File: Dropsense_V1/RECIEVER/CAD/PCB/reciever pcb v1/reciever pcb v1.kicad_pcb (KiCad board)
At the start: 2 copper layers, 50 x 60 mm, 27 parts, among them J1 1.8inch TFT connector, J2 USB_B_Micro, J3 Battery connector, SW1 EN SW, SW2 IO0 SW, U1 ESP32-S3-WROOM-1, U2 TP4056, U3 ME6211

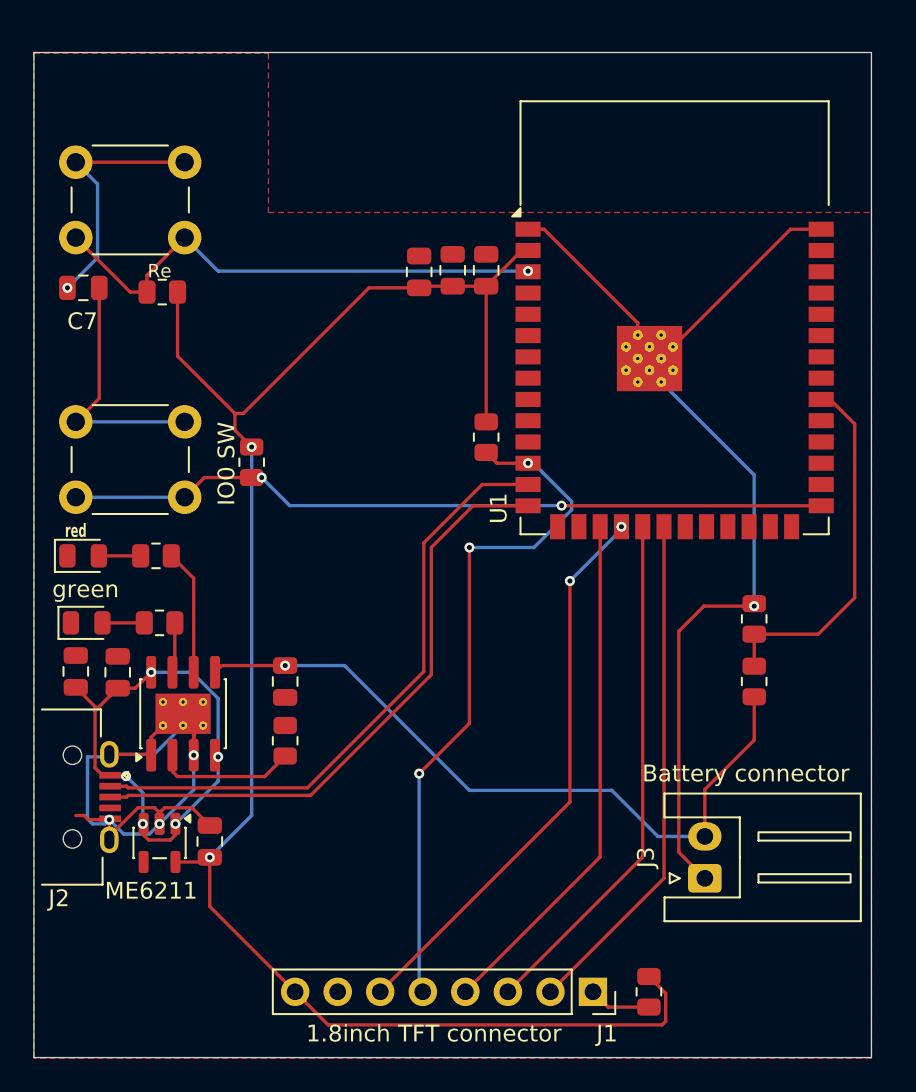
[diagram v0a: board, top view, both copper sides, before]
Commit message: PCB improvement
updated and polished both the pcbs of the sender and reciever mainly woked on moving viases away from smd components
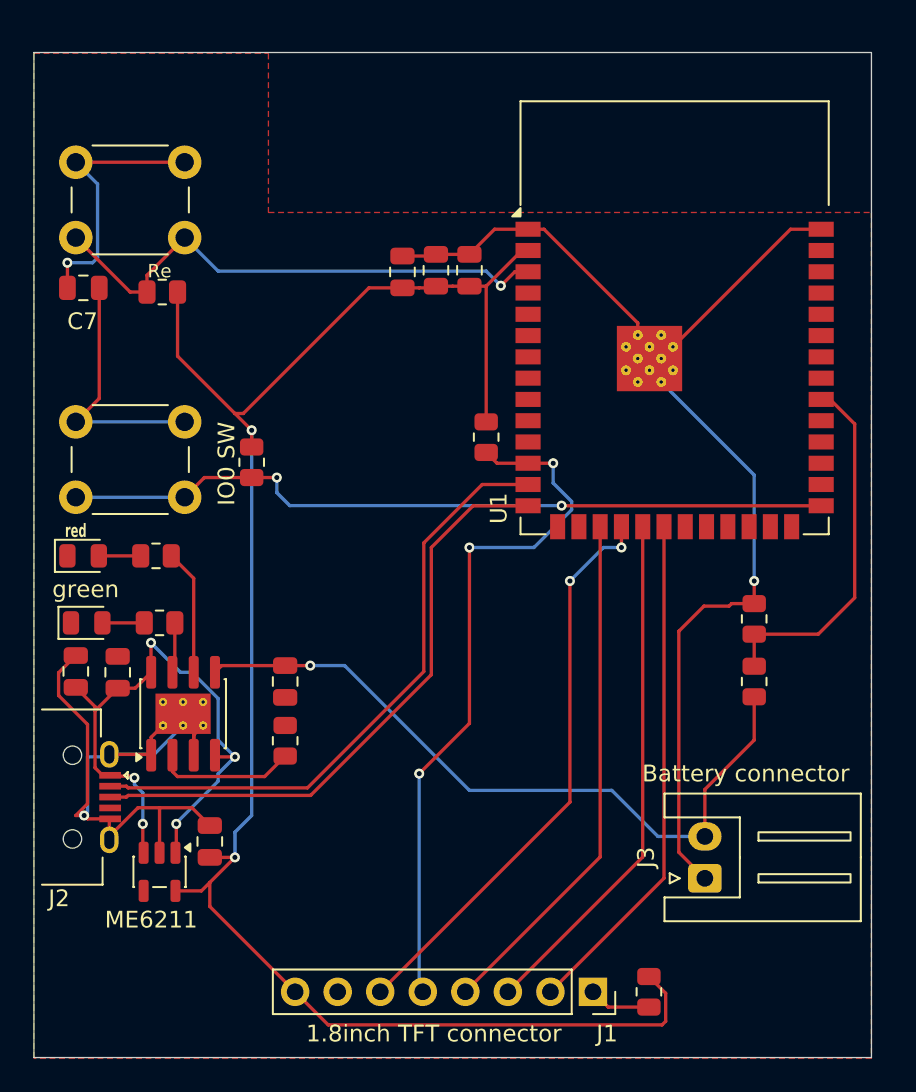
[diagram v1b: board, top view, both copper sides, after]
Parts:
- moved U3 1.72 mm to (109.5, 97.9)
- moved C4 1.00 mm to (124.0, 62.0)
- moved C5 1.00 mm to (126.0, 62.0)
- moved C6 1.00 mm to (128.0, 62.0)
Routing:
- net GND: track 114.7 -> 126.6 mm, vias 4 -> 2
- net /5V: track 31.9 -> 36.4 mm
- net 3v3: track 104.7 -> 107.6 mm
- net IO0: track 45.1 -> 46.2 mm
- net Net-(C7-Pad1): track 15.3 -> 16.2 mm
- net RESET: track 41.7 -> 42.4 mm
- net EN: track 31.1 -> 31.8 mm
- net CS: track 33.7 -> 34.4 mm

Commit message: made the 3d design and assembly
made the 3d design and assembly  for dropsense reciever
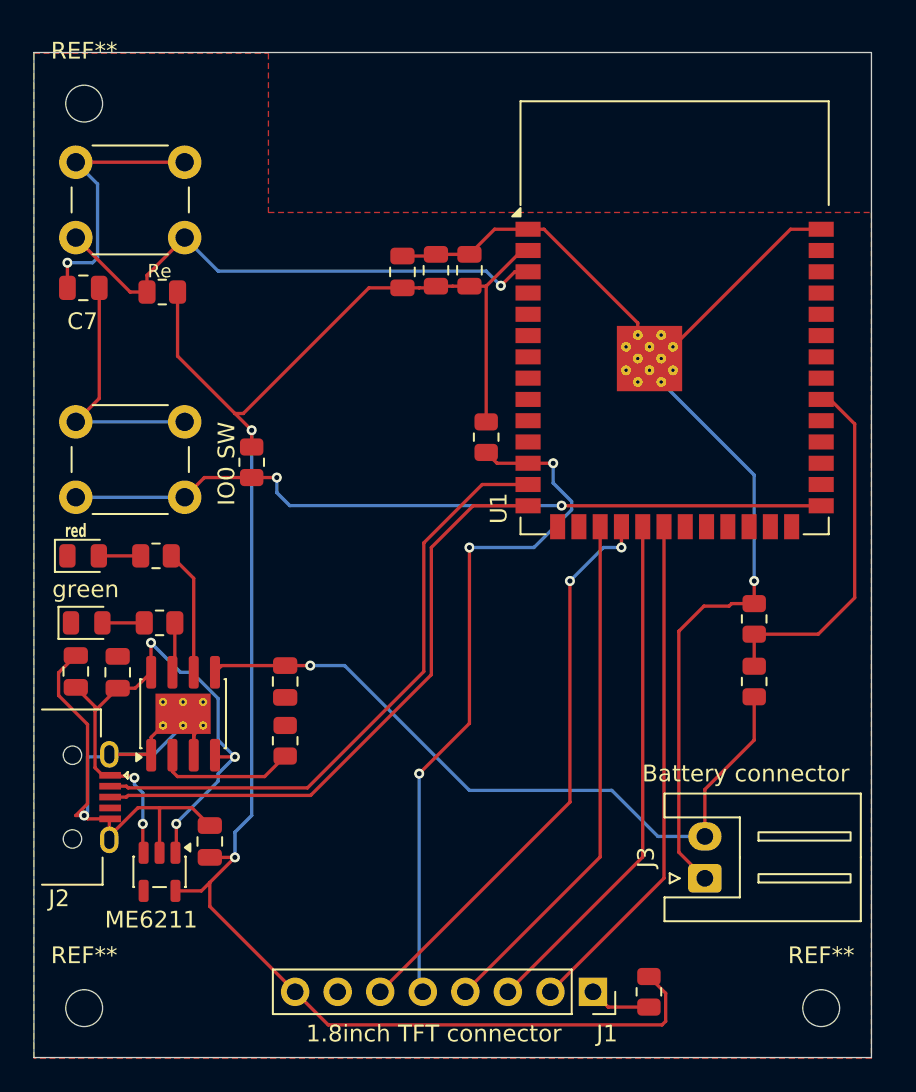
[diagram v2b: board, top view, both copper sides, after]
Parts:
- added REF**: MountingHole_2.2mm_M2, MountingHole:MountingHole_2.2mm_M2, F.Cu at (105.0, 106.0)
- added REF**: MountingHole_2.2mm_M2, MountingHole:MountingHole_2.2mm_M2, F.Cu at (149.0, 106.0)
- added REF**: MountingHole_2.2mm_M2, MountingHole:MountingHole_2.2mm_M2, F.Cu at (105.0, 52.0)
